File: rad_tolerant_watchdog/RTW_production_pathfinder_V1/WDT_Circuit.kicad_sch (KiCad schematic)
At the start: 27 parts, among them J1 Breakout, J15 Breakout, U1 TLV1704

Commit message: RTW V1 Pathfinder Layout Completed
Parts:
- added J18: Breakout, Connector_PinHeader_2.54mm:PinHeader_1x04_P2.54mm_Vertical, symbol Connector_Generic:Conn_01x04
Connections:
- net GND: now also J18.3 (Pin_3), J18.4 (Pin_4)
- net WDT_WDI_1: now also J18.1 (Pin_1), J18.2 (Pin_2)
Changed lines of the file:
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@@
 	)
 	(junction
+		(at 46.99 124.46)
+		(diameter 0)
+		(color 0 0 0 0)
+	)
+	(junction
 		(at 200.66 124.46)
 		(diameter 0)
@@
 	)
 	(junction
+		(at 46.99 132.08)
+		(diameter 0)
+		(color 0 0 0 0)
+	)
+	(junction
 		(at 132.08 124.46)
 		(diameter 0)
@@
 	(wire
 		(pts
+			(xy 46.99 116.84) (xy 46.99 124.46)
+		)
+		(stroke
+			(width 0)
+			(type default)
+		)
+	)
+	(wire
+		(pts
 			(xy 189.23 144.78) (xy 193.04 144.78)
 		)
@@
 	(wire
 		(pts
+			(xy 46.99 129.54) (xy 46.99 132.08)
+		)
+		(stroke
+			(width 0)
+			(type default)
+		)
+	)
+	(wire
+		(pts
 			(xy 200.66 144.78) (xy 200.66 137.16)
 		)
@@
 	(wire
 		(pts
+			(xy 46.99 132.08) (xy 46.99 137.16)
+		)
+		(stroke
+			(width 0)
+			(type default)
+		)
+	)
+	(wire
+		(pts
 			(xy 85.09 93.98) (xy 106.68 93.98)
 		)
@@
 	(wire
 		(pts
+			(xy 46.99 124.46) (xy 46.99 127)
+		)
+		(stroke
+			(width 0)
+			(type default)
+		)
+	)
+	(wire
+		(pts
 			(xy 30.48 30.48) (xy 33.02 30.48)
 		)
@@
 	(wire
 		(pts
+			(xy 46.99 127) (xy 50.8 127)
+		)
+		(stroke
+			(width 0)
+			(type default)
+		)
+	)
+	(wire
+		(pts
 			(xy 24.13 30.48) (xy 24.13 34.29)
 		)
@@
 	(wire
 		(pts
+			(xy 50.8 129.54) (xy 46.99 129.54)
+		)
+		(stroke
+			(width 0)
+			(type default)
+		)
+	)
+	(wire
+		(pts
 			(xy 85.09 86.36) (xy 140.97 86.36)
 		)
@@
 	(wire
 		(pts
+			(xy 46.99 124.46) (xy 50.8 124.46)
+		)
+		(stroke
+			(width 0)
+			(type default)
+		)
+	)
+	(wire
+		(pts
 			(xy 166.37 134.62) (xy 166.37 133.35)
 		)
@@
 	(wire
 		(pts
+			(xy 50.8 132.08) (xy 46.99 132.08)
+		)
+		(stroke
+			(width 0)
+			(type default)
+		)
+	)
+	(wire
+		(pts
 			(xy 85.09 78.74) (xy 208.28 78.74)
 		)
@@
 		)
 	)
+	(global_label "WDT_WDI_1"
+		(shape input)
+		(at 46.99 116.84 90)
+		(fields_autoplaced yes)
+		(effects
+			(font
+				(size 1.27 1.27)
+			)
+			(justify left)
+		)
+		(property "Intersheetrefs" "${INTERSHEET_REFS}"
+			(at 46.99 103.6949 90)
+			(effects
+				(font
+					(size 1.27 1.27)
+				)
+				(justify left)
+				(hide yes)
+			)
+		)
+	)
 	(global_label "~{RESET_1}"
 		(shape output)
@@
 	)
 	(symbol
+		(lib_id "Connector_Generic:Conn_01x04")
+		(at 55.88 127 0)
+		(unit 1)
+		(exclude_from_sim no)
+		(in_bom yes)
+		(on_board yes)
+		(dnp no)
+		(fields_autoplaced yes)
+		(property "Reference" "J18"
+			(at 58.42 126.9999 0)
+			(effects
+				(font
+					(size 1.27 1.27)
+				)
+				(justify left)
+			)
+		)
+		(property "Value" "Breakout"
+			(at 58.42 129.5399 0)
+			(effects
+				(font
+					(size 1.27 1.27)
+				)
+				(justify left)
+			)
+		)
+		(property "Footprint" "Connector_PinHeader_2.54mm:PinHeader_1x04_P2.54mm_Vertical"
+			(at 55.88 127 0)
+			(effects
+				(font
+					(size 1.27 1.27)
+				)
+				(hide yes)
+			)
+		)
+		(property "Datasheet" "~"
+			(at 55.88 127 0)
+			(effects
+				(font
+					(size 1.27 1.27)
+				)
+				(hide yes)
+			)
+		)
+		(property "Description" ""
+			(at 55.88 127 0)
+			(effects
+				(font
+					(size 1.27 1.27)
+				)
+				(hide yes)
+			)
+		)
+		(pin "1"
+		)
+		(pin "2"
+		)
+		(pin "3"
+		)
+		(pin "4"
+		)
+		(instances
+			(project "RTW_production_pathfinder_V1"
+				(path "/1ee67691-a73d-451f-9fc6-f9f8182134e0/0991a10f-8049-4fa6-be1f-88f50d17bad6"
+					(reference "J18")
+					(unit 1)
+				)
+			)
+		)
+	)
+	(symbol
 		(lib_id "power:GND")
 		(at 213.36 104.14 0)
@@
 					(unit 1)
 				)
+			)
+		)
+	)
+	(symbol
+		(lib_name "GND_1")
+		(lib_id "power:GND")
+		(at 46.99 137.16 0)
+		(unit 1)
+		(exclude_from_sim no)
+		(in_bom yes)
+		(on_board yes)
+		(dnp no)
+		(fields_autoplaced yes)
+		(property "Reference" "#PWR0107"
+			(at 46.99 143.51 0)
+			(effects
+				(font
+					(size 1.27 1.27)
+				)
+				(hide yes)
+			)
+		)
+		(property "Value" "GND"
+			(at 46.99 143.51 0)
+			(effects
+				(font
+					(size 1.27 1.27)
+				)
+			)
+		)
+		(property "Footprint" ""
+			(at 46.99 137.16 0)
+			(effects
+				(font
+					(size 1.27 1.27)
+				)
+				(hide yes)
+			)
+		)
+		(property "Datasheet" ""
+			(at 46.99 137.16 0)
+			(effects
+				(font
+					(size 1.27 1.27)
+				)
+				(hide yes)
+			)
+		)
+		(property "Description" "Power symbol creates a global label with name \"GND\" , ground"
+			(at 46.99 137.16 0)
+			(effects
+				(font
+					(size 1.27 1.27)
+				)
+				(hide yes)
+			)
+		)
+		(pin "1"
+		)
+		(instances
+			(project "RTW_production_pathfinder_V1"
+				(path "/1ee67691-a73d-451f-9fc6-f9f8182134e0/0991a10f-8049-4fa6-be1f-88f50d17bad6"
+					(reference "#PWR0107")
+					(unit 1)
+				)

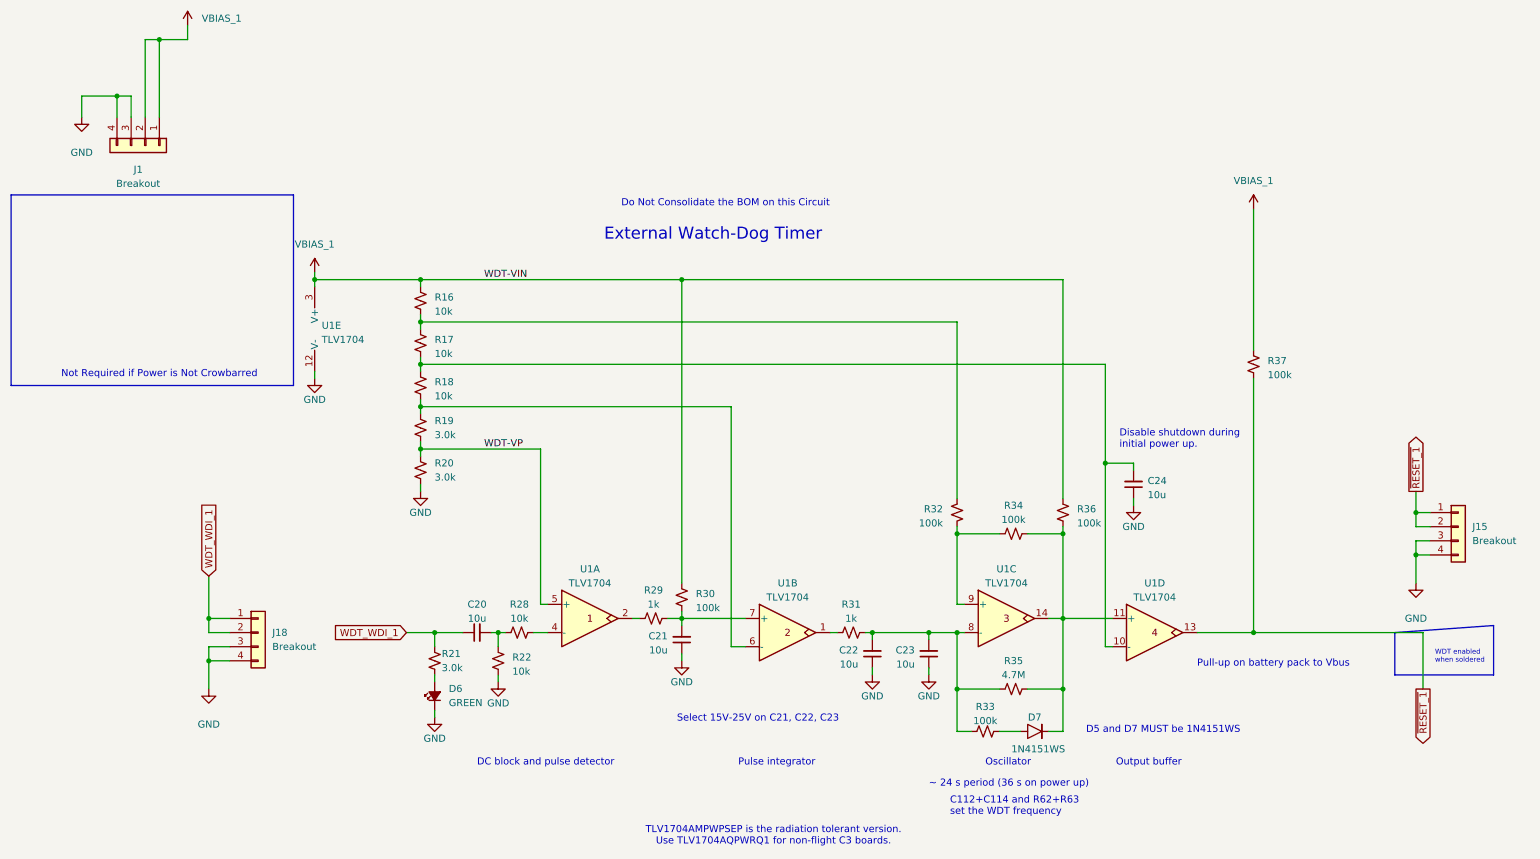
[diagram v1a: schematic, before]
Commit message: Added Decoupling Caps on VBIAS
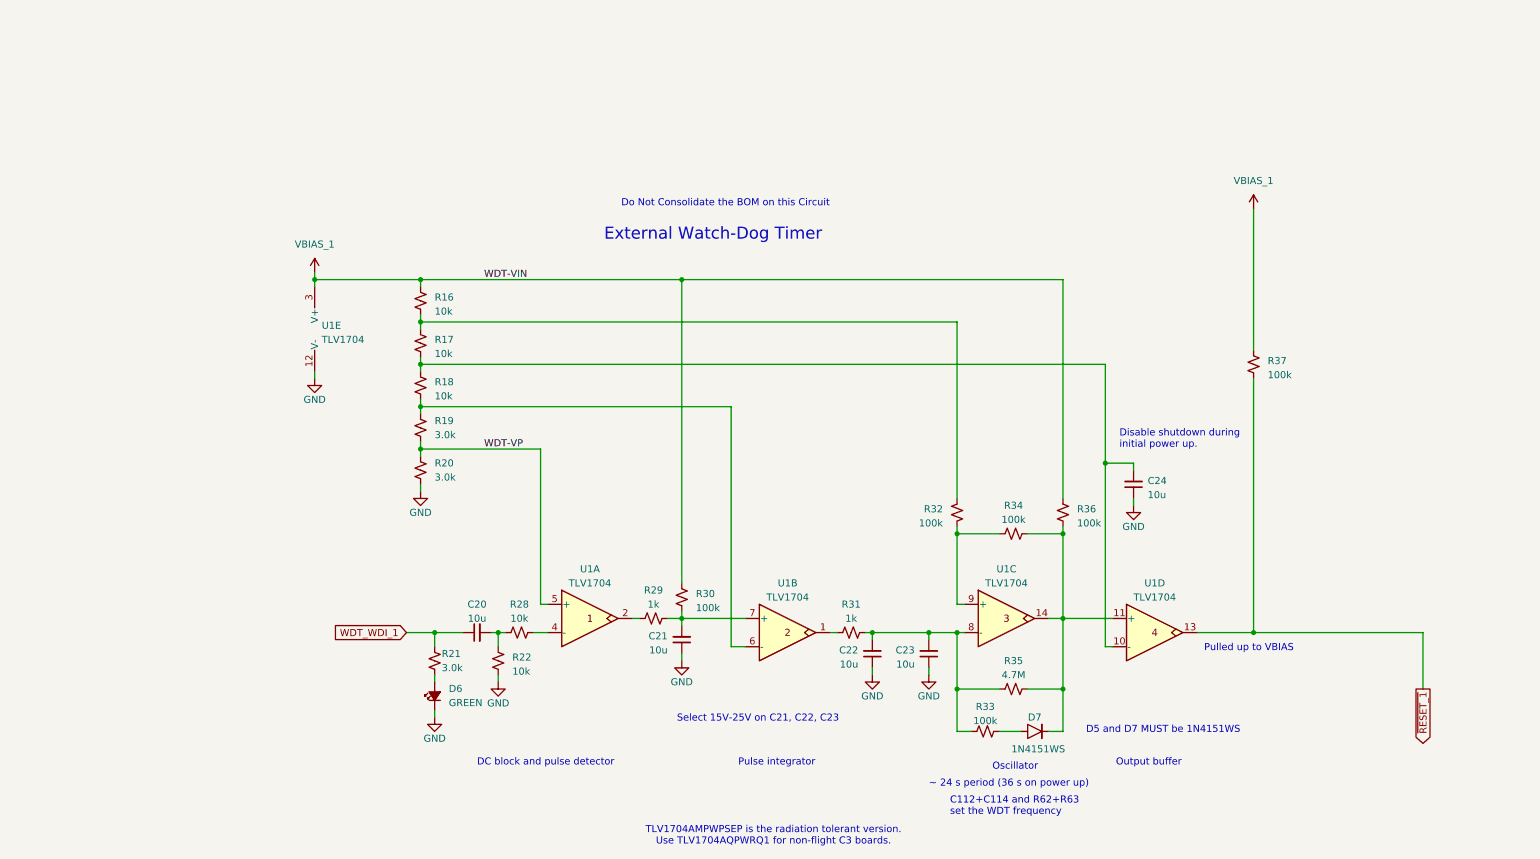
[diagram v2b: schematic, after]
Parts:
- removed J1, J15, J18: Breakout, Connector_PinHeader_2.54mm:PinHeader_1x04_P2.54mm_Vertical, symbol Connector_Generic:Conn_01x04
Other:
- note added: "Pulled up to VBIAS"
- note removed: "Not Required if Power is Not Crowbarred"
- note removed: "Pull-up on battery pack to Vbus"
- note removed: "WDT enabled when soldered"

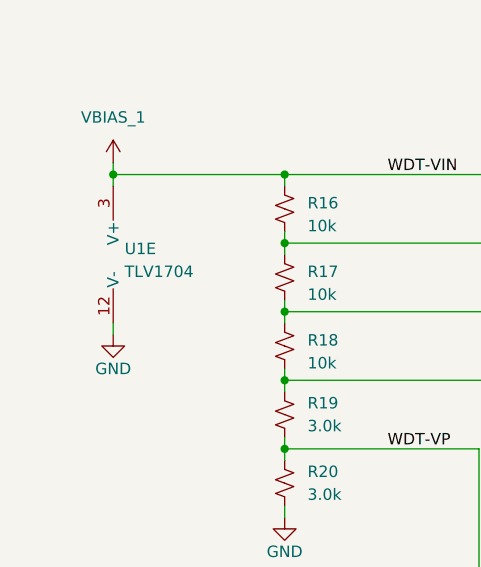
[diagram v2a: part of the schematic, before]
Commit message: Added Bypass Caps to WDT 1 & 2
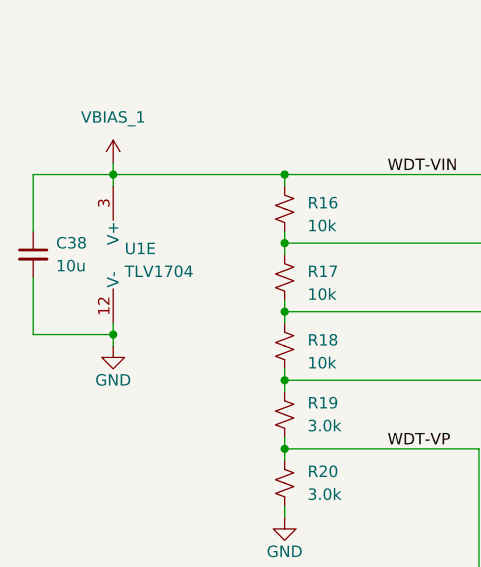
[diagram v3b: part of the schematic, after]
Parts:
- added C38: 10u, Capacitor_SMD:C_0603_1608Metric, symbol Device:C_Small
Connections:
- net GND: now also C38.2
- net VBIAS_1: now also C38.1
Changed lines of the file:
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@@
+	)
+	(junction
+		(at 66.04 81.28)
+		(diameter 0)
+		(color 0 0 0 0)
 	)
 	(junction
@@
 	(wire
 		(pts
+			(xy 57.15 74.93) (xy 57.15 81.28)
+		)
+		(stroke
+			(width 0)
+			(type default)
+		)
+	)
+	(wire
+		(pts
 			(xy 182.88 121.92) (xy 181.61 121.92)
 		)
@@
 	(wire
 		(pts
+			(xy 66.04 81.28) (xy 66.04 80.01)
+		)
+		(stroke
+			(width 0)
+			(type default)
+		)
+	)
+	(wire
+		(pts
 			(xy 181.61 121.92) (xy 181.61 109.22)
 		)
@@
 	(wire
 		(pts
+			(xy 66.04 82.55) (xy 66.04 81.28)
+		)
+		(stroke
+			(width 0)
+			(type default)
+		)
+	)
+	(wire
+		(pts
 			(xy 181.61 109.22) (xy 189.23 109.22)
 		)
@@
 	(wire
 		(pts
+			(xy 66.04 63.5) (xy 57.15 63.5)
+		)
+		(stroke
+			(width 0)
+			(type default)
+		)
+	)
+	(wire
+		(pts
 			(xy 189.23 137.16) (xy 181.61 137.16)
 		)
@@
 	(wire
 		(pts
-			(xy 66.04 81.28) (xy 66.04 80.01)
-		)
-		(stroke
-			(width 0)
-			(type default)
-		)
-	)
-	(wire
-		(pts
 			(xy 198.12 124.46) (xy 200.66 124.46)
 		)
@@
 		(pts
 			(xy 194.31 109.22) (xy 200.66 109.22)
+		)
+		(stroke
+			(width 0)
+			(type default)
+		)
+	)
+	(wire
+		(pts
+			(xy 57.15 81.28) (xy 66.04 81.28)
+		)
+		(stroke
+			(width 0)
+			(type default)
+		)
+	)
+	(wire
+		(pts
+			(xy 57.15 63.5) (xy 57.15 69.85)
 		)
 		(stroke
@@
 					(reference "U1")
 					(unit 5)
+				)
+			)
+		)
+	)
+	(symbol
+		(lib_id "Device:C_Small")
+		(at 57.15 72.39 0)
+		(unit 1)
+		(exclude_from_sim no)
+		(in_bom yes)
+		(on_board yes)
+		(dnp no)
+		(fields_autoplaced yes)
+		(property "Reference" "C38"
+			(at 59.69 71.1262 0)
+			(effects
+				(font
+					(size 1.27 1.27)
+				)
+				(justify left)
+			)
+		)
+		(property "Value" "10u"
+			(at 59.69 73.6662 0)
+			(effects
+				(font
+					(size 1.27 1.27)
+				)
+				(justify left)
+			)
+		)
+		(property "Footprint" "Capacitor_SMD:C_0603_1608Metric"
+			(at 57.15 72.39 0)
+			(effects
+				(font
+					(size 1.27 1.27)
+				)
+				(hide yes)
+			)
+		)
+		(property "Datasheet" "~"
+			(at 57.15 72.39 0)
+			(effects
+				(font
+					(size 1.27 1.27)
+				)
+				(hide yes)
+			)
+		)
+		(property "Description" "10 µF ±10% 16V Ceramic Capacitor X5R 0603 (1608 Metric)"
+			(at 57.15 72.39 0)
+			(effects
+				(font
+					(size 1.27 1.27)
+				)
+				(hide yes)
+			)
+		)
+		(property "DPN" "490-12317-1-ND"
+			(at 57.15 72.39 0)
+			(effects
+				(font
+					(size 1.27 1.27)
+				)
+				(hide yes)
+			)
+		)
+		(property "DST" "Digi-Key"
+			(at 57.15 72.39 0)
+			(effects
+				(font
+					(size 1.27 1.27)
+				)
+				(hide yes)
+			)
+		)
+		(property "MFR" "Murata"
+			(at 57.15 72.39 0)
+			(effects
+				(font
+					(size 1.27 1.27)
+				)
+				(hide yes)
+			)
+		)
+		(property "MPN" "GRT188R61C106KE13D"
+			(at 57.15 72.39 0)
+			(effects
+				(font
+					(size 1.27 1.27)
+				)
+				(hide yes)
+			)
+		)
+		(pin "1"
+		)
+		(pin "2"
+		)
+		(instances
+			(project "RTW_production_pathfinder_V1"
+				(path "/1ee67691-a73d-451f-9fc6-f9f8182134e0/0991a10f-8049-4fa6-be1f-88f50d17bad6"
+					(reference "C38")
+					(unit 1)
 				)
 			)
@@
 	(symbol
 		(lib_id "power:GND")
-		(at 66.04 81.28 0)
+		(at 66.04 82.55 0)
 		(mirror y)
 		(unit 1)
@@
 		(dnp no)
 		(property "Reference" "#PWR045"
-			(at 66.04 87.63 0)
+			(at 66.04 88.9 0)
 			(effects
 				(font
@@
 		)
 		(property "Value" "GND"
-			(at 66.04 85.09 0)
+			(at 66.04 86.36 0)
 			(effects
 				(font
@@
 		)
 		(property "Footprint" ""
-			(at 66.04 81.28 0)
+			(at 66.04 82.55 0)
 			(effects
 				(font
@@
 		)
 		(property "Datasheet" ""
-			(at 66.04 81.28 0)
+			(at 66.04 82.55 0)
 			(effects
 				(font
@@
 		)
 		(property "Description" "Power symbol creates a global label with name \"GND\" , ground"
-			(at 66.04 81.28 0)
-			(effects
-				(font
+			(at 66.04 82.55 0)
+			(effects
+				(font
